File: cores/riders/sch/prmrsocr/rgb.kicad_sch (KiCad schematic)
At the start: 28 parts

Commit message: wip prmrsocr: Sound
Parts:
- removed C14: 74LS04, symbol jt74:74LS04
- removed C15, C16, C17, C19, C20, E19: 74LS07, symbol 74xx:74LS07
- removed E16: 74LS00, symbol jt74:74LS00
- removed F20: 74LS164, symbol jt74:74LS164
- removed R12, R15, R16, R17, R19, R21, R23, R24, R25, R26, R27: N.M, symbol Device:R_US
- removed R22: 118 Ohm, symbol Device:R_US
- added 10G: 74LS04, symbol jt74:74LS04
- added 7B1, 7B41, 8B, 9B: 74LS07, symbol 74xx:74LS07
- added 7J41: 74LS08, symbol jt74:74LS08
- added R41, R42: 3300 Ohm, symbol Device:R_US
- added R43: 3300 Omh, symbol Device:R_US
- renumbered E20 to 10E, E21 to 11E1, D19 to 7D1, D20 to 7D2, S2 to R12, S3 to R13, S1 to R14
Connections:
- net ~{COCEH} is gone; now on net PALETTE~{CS}: 10E.19 (~{CE})
- net B0: now also 7D1.16 (Q6), 7B1.5; no longer 7D1.6 (Q2)
- net B1: now also 7D1.15 (Q5), 7B1.9; no longer 7D1.9 (Q3)
- net B2: now also 7B1.3
- net B3: now also 7D1.9 (Q3), 9B.9; no longer 7D1.15 (Q5)
- net B4: now also 7D1.6 (Q2), 7B1.1; no longer 7D1.16 (Q6)
- net G0: now also 7D1.5 (Q1), 9B.5; no longer 7D2.15 (Q5)
- net G1: now also 7D1.2 (Q0), 8B.13; no longer 7D2.16 (Q6)
- net G2: now also 9B.3
- net G3: now also 7D2.16 (Q6), 8B.11; no longer 7D1.2 (Q0)
- net G4: now also 7D2.15 (Q5), 9B.1; no longer 7D1.5 (Q1)
- net PALETTE~{CS}: now also 11E1.19 (~{CE})
- net R0: now also 7D2.12 (Q4), 8B.5; no longer 7D2.2 (Q0)
- net R1: now also 7D2.9 (Q3), 8B.9; no longer 7D2.5 (Q1)
- net R2: now also 9B.13
- net R3: now also 7D2.5 (Q1), 8B.3; no longer 7D2.9 (Q3)
- net R4: now also 7D2.2 (Q0), 9B.11; no longer 7D2.12 (Q4)
- net SDO0: now also 10G.9
- net ~{COCEL}: no longer 11E1.19 (~{CE})
- net ~{HBLANK}: now also 7J41.9
- net ~{SHADOW}: now also 7B41.13, 7B41.3, 7B41.5
- net ~{VBLANK}: now also 7J41.10
- net at R12.5 (D1): now also 8B.10
- net at R13.5 (D1): now also 8B.4
- net at R14.5 (D1): now also 9B.8
- net at R13.7 (BK): now also 7B1.10, R43.1
- net at R12.4 (D2): now also 9B.4
- net at R13.6 (D0): now also 9B.10
- net at R14.7 (BK): now also 7B1.12, R41.1
- net at R12.6 (D0): now also 9B.2
- net at R12.3 (D3): now also 8B.12
- net at R13.3 (D3): now also 8B.8
- net at R14.6 (D0): now also 7B1.2
- net at R12.2 (D4): now also 9B.6
- net at R12.7 (BK): now also 8B.2, R42.1
- net at R13.2 (D4): now also 8B.6
- net at R14.3 (D3): now also 7B1.8
- net at R14.2 (D4): now also 7B1.6
- net at R14.4 (D2): now also 7B1.4
- net at R13.4 (D2): now also 9B.12
- net at 7D1.18 (D7): now also 10G.8
- new net: 7B1.11, 7B1.13, 7J41.8, 8B.1
- new net: 7B41.6, R42.2
- new net: 7B41.4, R41.2
- new net: 7B41.12, R43.2
- no-connect marks 7 -> 0
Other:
- note removed: "USED IN THE GAME LETHAL ENFORCERS"
- moved on the sheet: R12, R13

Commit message: wip prmrsocr: root
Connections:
- net PALETTE~{CS}: no longer 10E.1 (A->B), 11E1.1 (A->B)
- new net ~{RD}: 10E.1 (A->B), 11E1.1 (A->B)
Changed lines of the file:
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@@
-		)
-	)
-	(label "~{RD}"
-		(at 55.88 115.57 0)
-		(effects
-			(font
-				(size 1.27 1.27)
-			)
-			(justify left bottom)
 		)
 	)
@@
 	(label "RGB11"
 		(at 93.98 97.79 0)
-		(effects
-			(font
-				(size 1.27 1.27)
-			)
-			(justify left bottom)
-		)
-	)
-	(label "~{RD}"
-		(at 50.8 113.03 0)
 		(effects
 			(font
@@
 		(effects
 			(font
+				(size 1.27 1.27)
+			)
+			(justify right)
+		)
+	)
+	(hierarchical_label "~{RD}"
+		(shape input)
+		(at 50.8 113.03 180)
+		(effects
+			(font

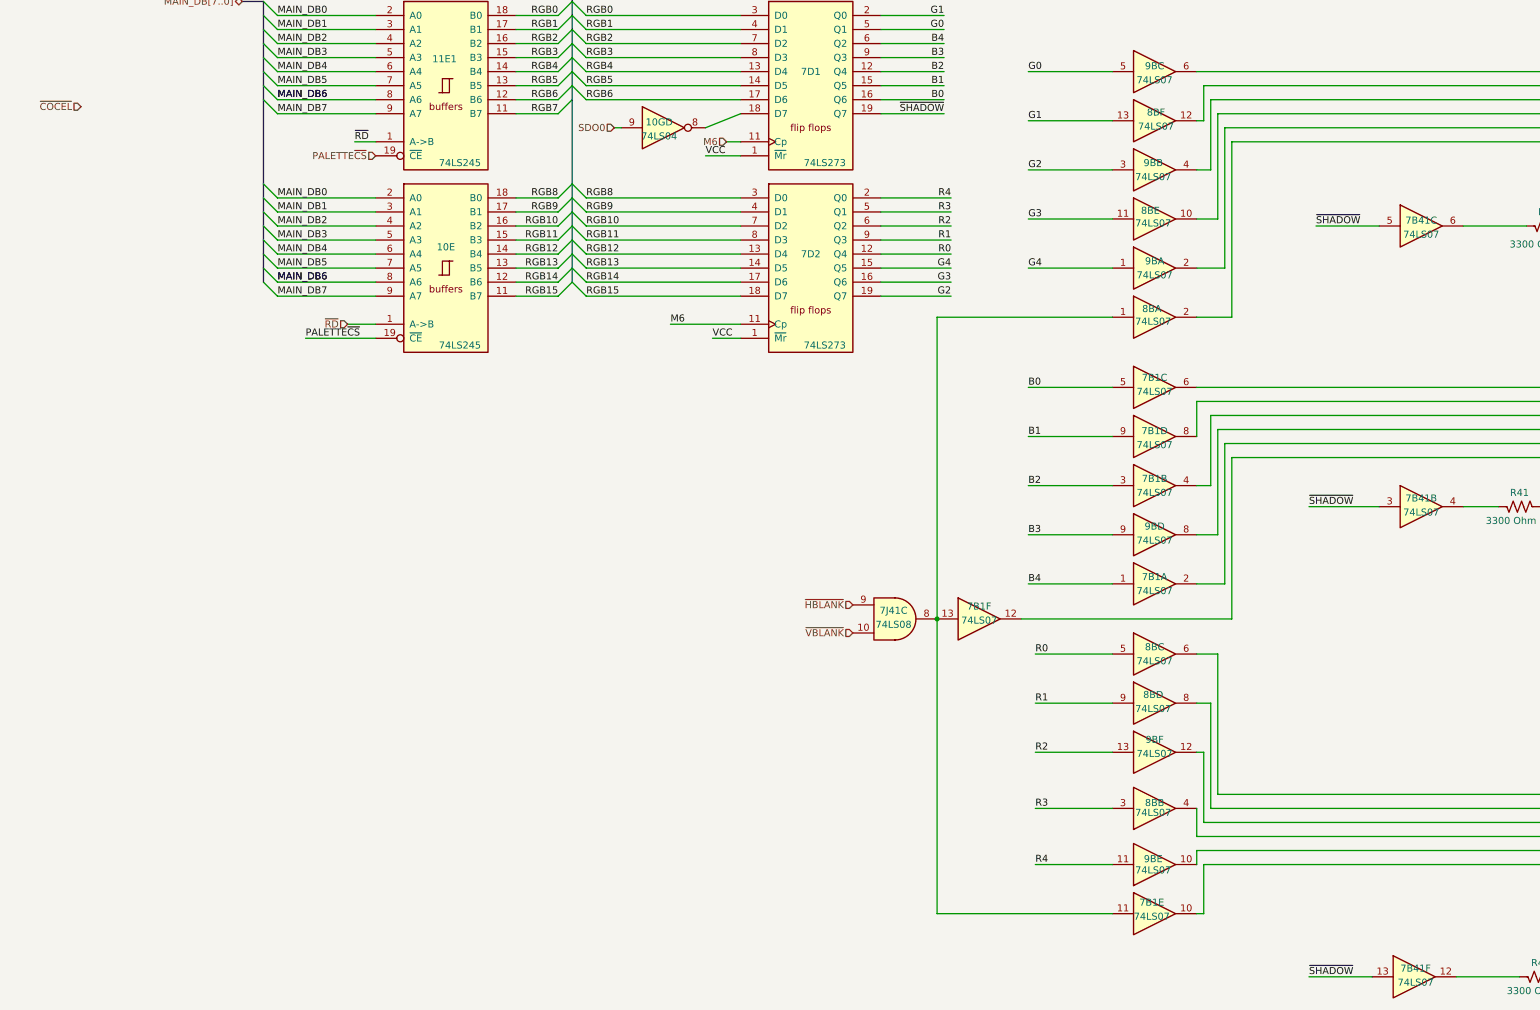
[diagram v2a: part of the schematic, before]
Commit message: sch prmrsocr no errors
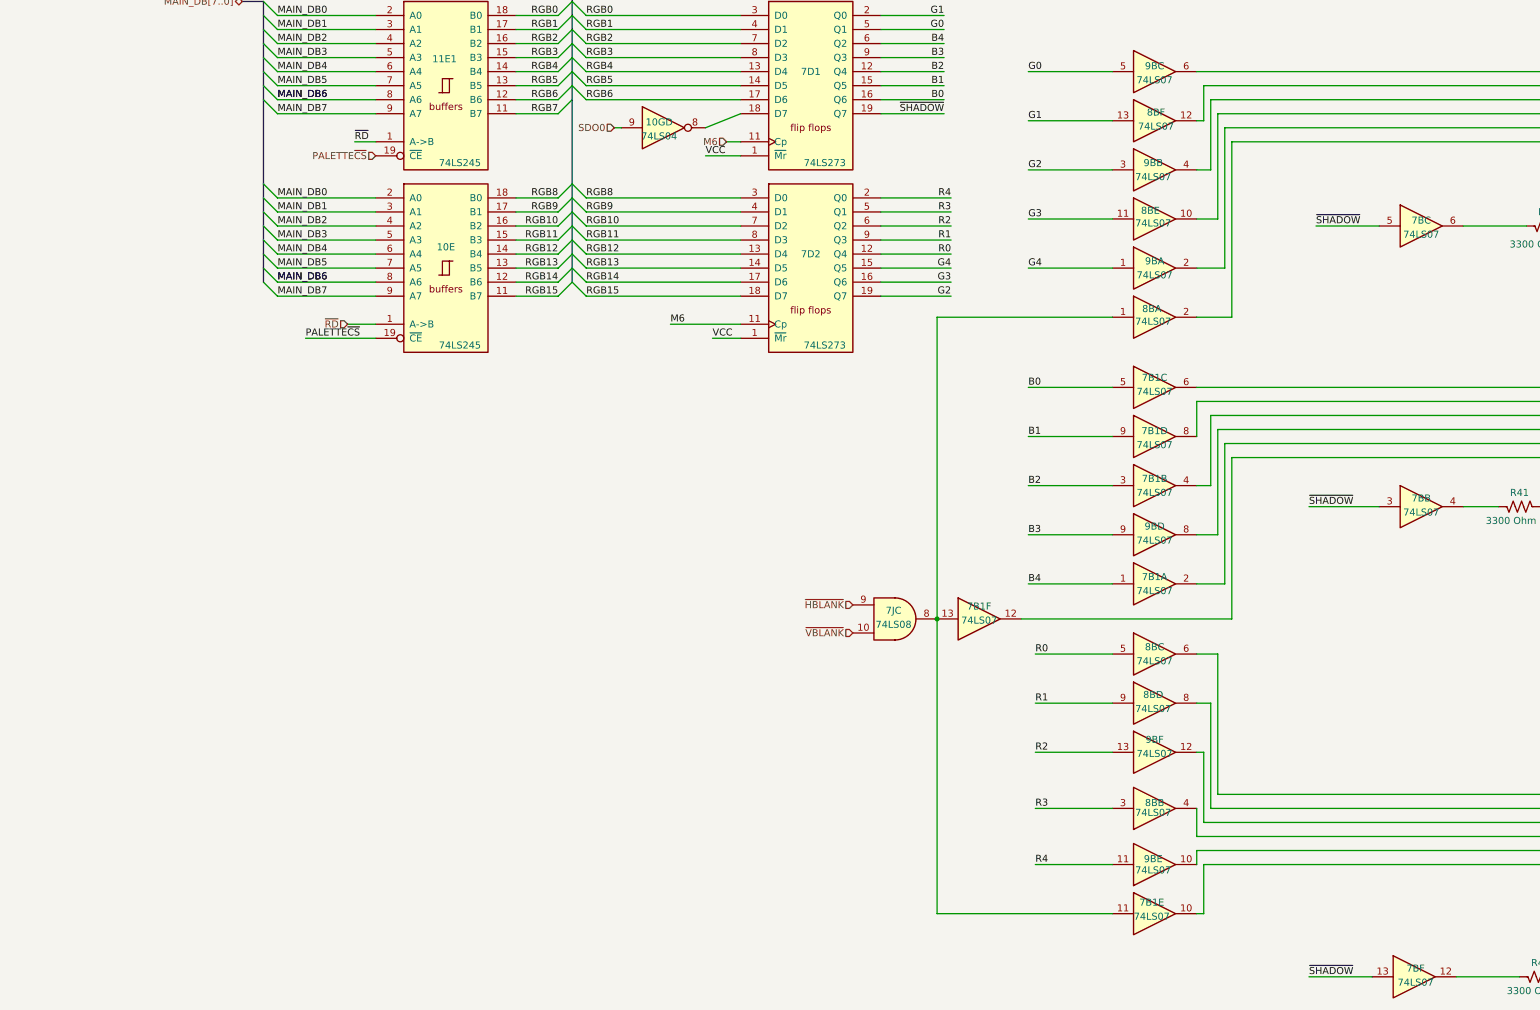
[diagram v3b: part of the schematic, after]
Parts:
- renumbered 7B41 to 7B, 7J41 to 7J
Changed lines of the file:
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@@
-		)
-	)
-	(hierarchical_label "~{COCEL}"
-		(shape input)
-		(at 2.54 73.66 180)
-		(effects
-			(font
-				(size 1.27 1.27)
-			)
-			(justify right)
 		)
 	)
@@
 		(on_board yes)
 		(dnp no)
-		(property "Reference" "7J41"
+		(property "Reference" "7J"
 			(at 149.606 164.846 0)
 			(effects
@@
 			(project "prmrsocr"
 				(path "/0011ec10-82c4-4039-b424-337480f568e8/f4542c68-089e-4b0f-a6b3-8df02e621902/a6774e1c-13eb-4aac-8698-807248f75e99"
-					(reference "7J41")
+					(reference "7J")
 					(unit 3)
 				)
@@
 		(on_board yes)
 		(dnp no)
-		(property "Reference" "7B41"
+		(property "Reference" "7B"
 			(at 245.11 94.234 0)
 			(effects
@@
 			(project "prmrsocr"
 				(path "/0011ec10-82c4-4039-b424-337480f568e8/f4542c68-089e-4b0f-a6b3-8df02e621902/a6774e1c-13eb-4aac-8698-807248f75e99"
-					(reference "7B41")
+					(reference "7B")
 					(unit 3)
 				)
@@
 		(on_board yes)
 		(dnp no)
-		(property "Reference" "7B41"
+		(property "Reference" "7B"
 			(at 244.094 229.616 0)
 			(effects
@@
 			(project "prmrsocr"
 				(path "/0011ec10-82c4-4039-b424-337480f568e8/f4542c68-089e-4b0f-a6b3-8df02e621902/a6774e1c-13eb-4aac-8698-807248f75e99"
-					(reference "7B41")
+					(reference "7B")
 					(unit 6)
 				)
@@
 		(on_board yes)
 		(dnp no)
-		(property "Reference" "7B41"
+		(property "Reference" "7B"
 			(at 245.11 144.526 0)
 			(effects
@@
 			(project "prmrsocr"
 				(path "/0011ec10-82c4-4039-b424-337480f568e8/f4542c68-089e-4b0f-a6b3-8df02e621902/a6774e1c-13eb-4aac-8698-807248f75e99"
-					(reference "7B41")
+					(reference "7B")
 					(unit 2)
 				)

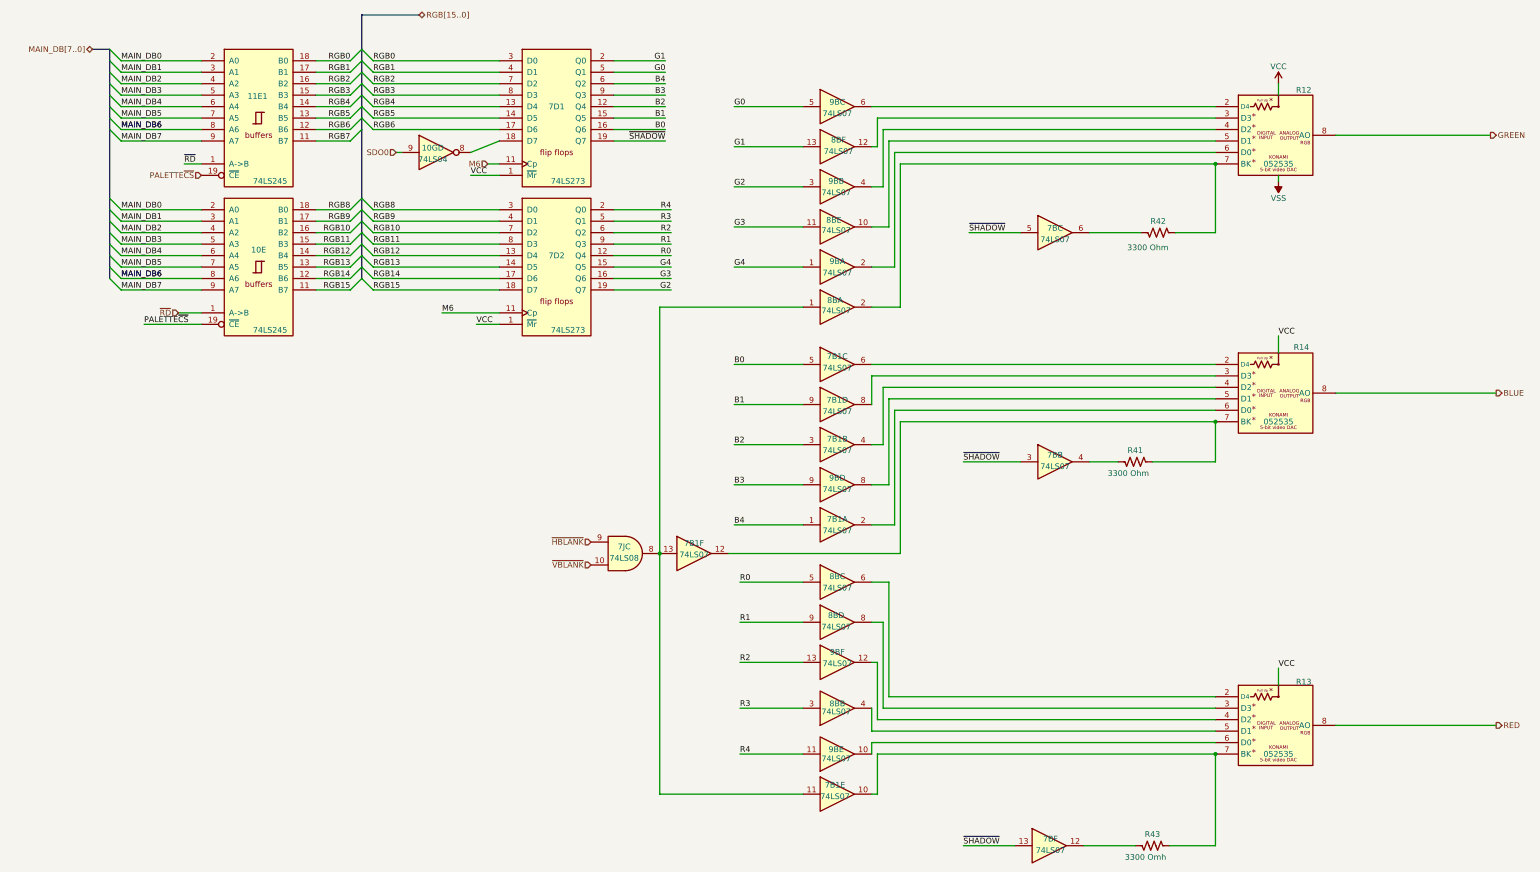
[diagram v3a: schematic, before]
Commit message: Prmrsocr sch + 054986 sheet  (#1300)
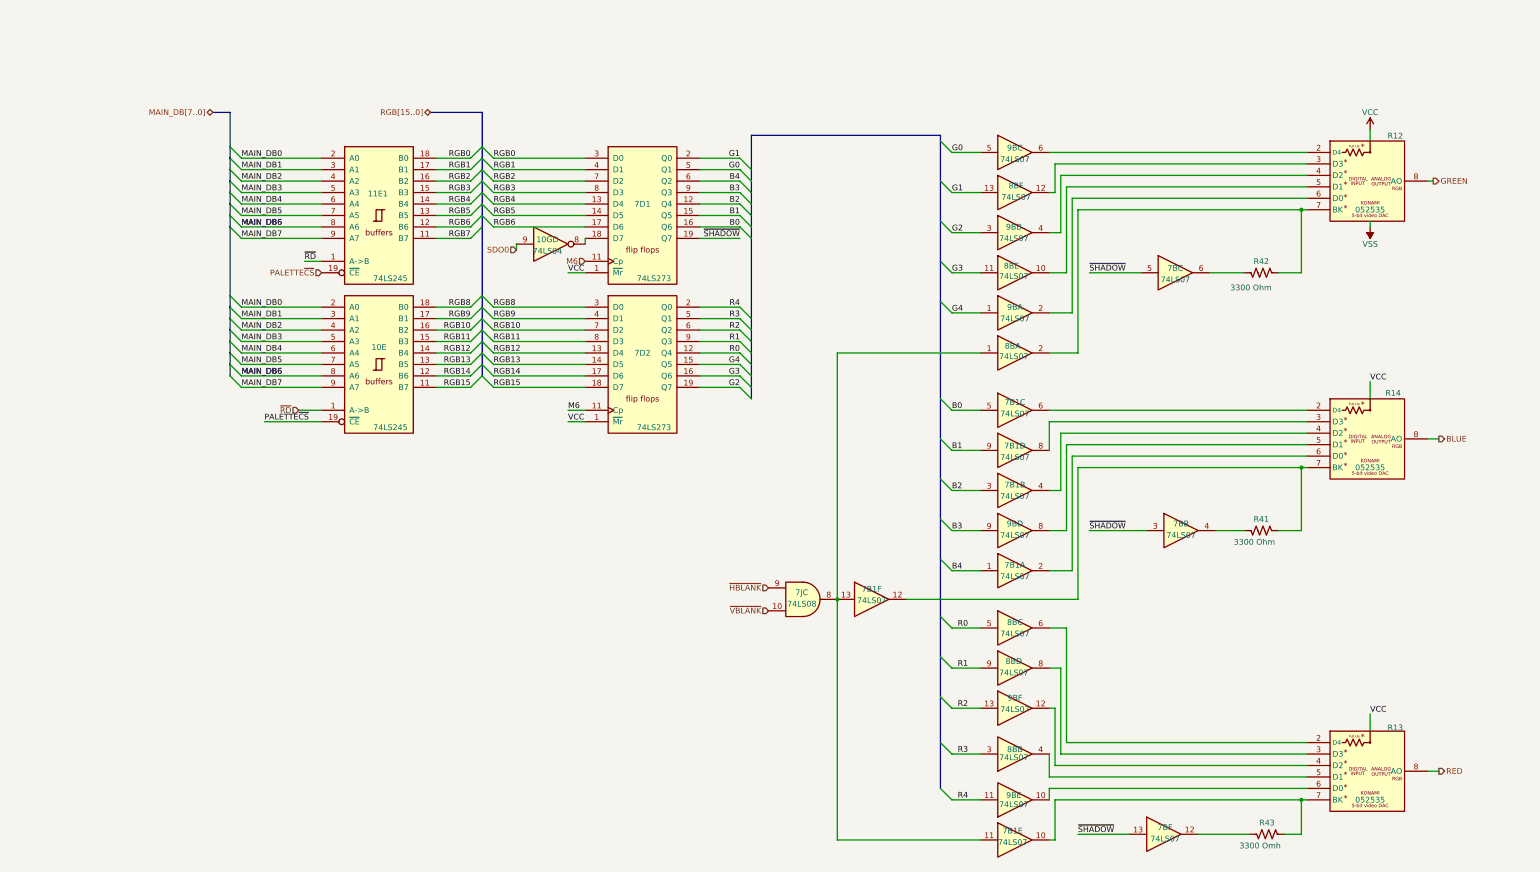
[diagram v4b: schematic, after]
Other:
- moved on the sheet: 10E, 10GD, 11E1, 7B1A, 7B1B, 7B1C, 7B1D, 7B1E, 7B1F, 7BB, 7BC, 7BF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
